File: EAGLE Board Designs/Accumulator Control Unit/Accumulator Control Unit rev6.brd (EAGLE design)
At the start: 255 x 73 mm, 301 parts, among them J1 CONNECTOR-12_MF_T_V_, J2 CONNECTOR-6_μF_T_V_BLACK, J3 CONNECTOR-4_μF_T_V_BLACK, J4 CONNECTOR-2_MF_T_V_, J5 CONNECTOR-8_μF_T_V_BLACK, J6 CONNECTOR-16_MF_T_V_, J9 CONNECTOR-2_MF_T_V_, Q1 TRANSISTOR_N_MOS__PMV15ENEA, Q2 TRANSISTOR_N_MOS__PMV15ENEA, Q3 TRANSISTOR_N_MOS__PMV15ENEA, Q4 TRANSISTOR_N_MOS__PMV15ENEA, T1 TRANSFORMER_HM2112ZNLT_AIRGAP, U1 VOLTAGE_REGULATOR_SOT-223_3.3V, U10 TCAN1051HQV-Q1, U11 OPAMP_1_CHANNEL_OPA991, U12 OPAMP_1_CHANNEL_OPA991, U13 OPAMP_1_CHANNEL_OPA991, U14 RELAY_SOLIDSTATE_NO_DIP-4, U15 LM555, U16 OPAMP_1_CHANNEL_OPA991, U17 OPAMP_2_CHANNEL_OPA_2991, U18 OPAMP_1_CHANNEL_OPA991, U19 OPAMP_2_CHANNEL_OPA_2991, U2 RELAY_SOLIDSTATE_NO_DIP-4, U20 LOGICGATE_BUFFER, U21 ADM8316WBX30, U22 OPAMP_1_CHANNEL_OPA991, U23 LOGICGATE_AND_DCK3, U24 LOGICGATE_AND_DCK3, U25 LOGICGATE_AND_DCK3, U26 OPAMP_1_CHANNEL_OPA991, U27 ADG1423, U28 OPAMP_1_CHANNEL_OPA991, U29 OPAMP_2_CHANNEL_OPA_2991, U3 RELAY_SOLIDSTATE_NO_DIP-4, U30 OPAMP_1_CHANNEL_OPA991, U31 OPAMP_2_CHANNEL_OPA_2991, U32 LTC6820, U33 OPAMP_1_CHANNEL_OPA991, U4 OPAMP_1_CHANNEL_OPA991, U5 OPAMP_1_CHANNEL_OPA991, U6 TCAN1051HQV-Q1, U7 LTC6820, U8 OPAMP_1_CHANNEL_OPA991, U9 OPAMP_1_CHANNEL_OPA991

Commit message: acu_rev6_schematic_update
moved precharge control circuit difference amplifiers' pull down resistors to between the differential inputs
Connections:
- net GND: no longer R55.1, R62.1
- net ISO_PACK+: now also R55.2
- net ISO_PACK-: now also R55.1; no longer R55.2
- net ISO_TS+: now also R62.2
- net ISO_TS-: now also R62.1; no longer R62.2
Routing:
- net ISO_TS+: track 23.7 -> 20.8 mm
- net ISO_PACK+: track 24.8 -> 22.1 mm
- net GND: track 544.1 -> 541.5 mm, vias 132 -> 130
- net ISO_PACK-: track 23.8 -> 22.2 mm
- net ISO_TS-: track 21.0 -> 19.6 mm

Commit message: acu-rev6-schematic-update
some changes to precharge control circuit
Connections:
- net HV+_OUT_OK: now also R87.2, U23.4, U25.2; no longer R88.2, U24.4, U25.1
- net PRECHARGE+_OUT_OK: now also R88.2, U24.4, U25.1; no longer R87.2, U23.4, U25.2
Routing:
- net PRECHARGE+_OUT_OK: track 6.56 -> 21.6 mm
- net HV+_OUT_OK: track 21.6 -> 6.56 mm
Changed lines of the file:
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@@
 <wire x1="18.419" y1="8.3488" x2="19.8224" y2="8.3488" width="0.254" layer="1"/>
 </signal>
-<signal name="HV+_OUT_OK">
+<signal name="PRECHARGE+_OUT_OK">
 <contactref element="U24" pad="4"/>
 <contactref element="U25" pad="1"/>
@@
 <wire x1="16.6624" y1="15.7344" x2="16.6624" y2="16.2188" width="0.254" layer="1"/>
 </signal>
-<signal name="PRECHARGE+_OUT_OK">
+<signal name="HV+_OUT_OK">
 <contactref element="U23" pad="4"/>
 <contactref element="U25" pad="2"/>

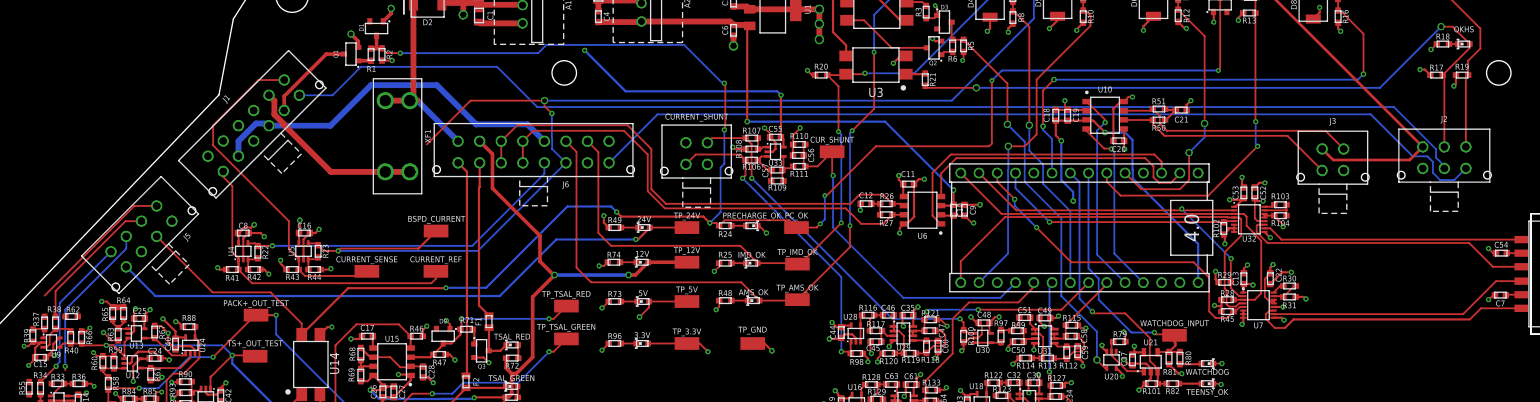
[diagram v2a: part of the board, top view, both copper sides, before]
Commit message: some routing fixed will do the rest once I get back
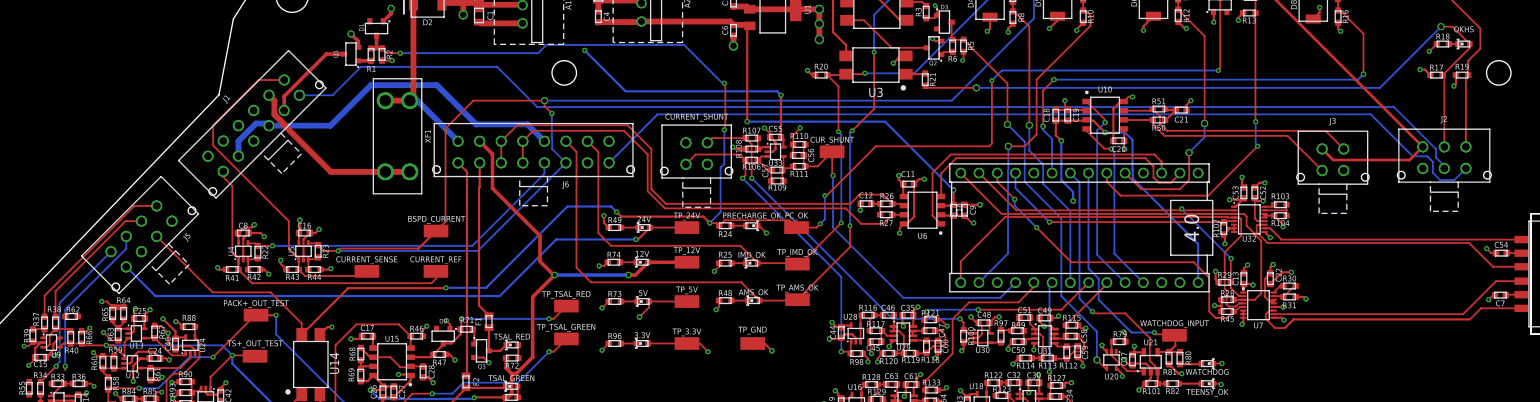
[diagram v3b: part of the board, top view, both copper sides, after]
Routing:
- net BSPD_CURRENT: track 168.9 -> 180.1 mm
- net ISO_TS+: track 20.8 -> 23.7 mm
- net 24VIN: track 27.3 -> 26.3 mm
- net WATCHDOG_INPUT: track 37.3 -> 36.7 mm
- net GND: track 541.5 -> 542.1 mm

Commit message: fixed all drc errrors again
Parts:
- moved R62 3.35 mm to (9.27, 24.8)
- moved R55 1.15 mm to (7.24, 14.3), turned to 0 degrees
- moved R34 1.04 mm to (7.24, 12.8), turned to 0 degrees
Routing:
- net ISO_PACK+: track 22.1 -> 26.3 mm
- net +24V: track 392.5 -> 388.4 mm
- net ISO_PACK-: track 22.2 -> 25.3 mm
- net GND: track 542.1 -> 542.8 mm

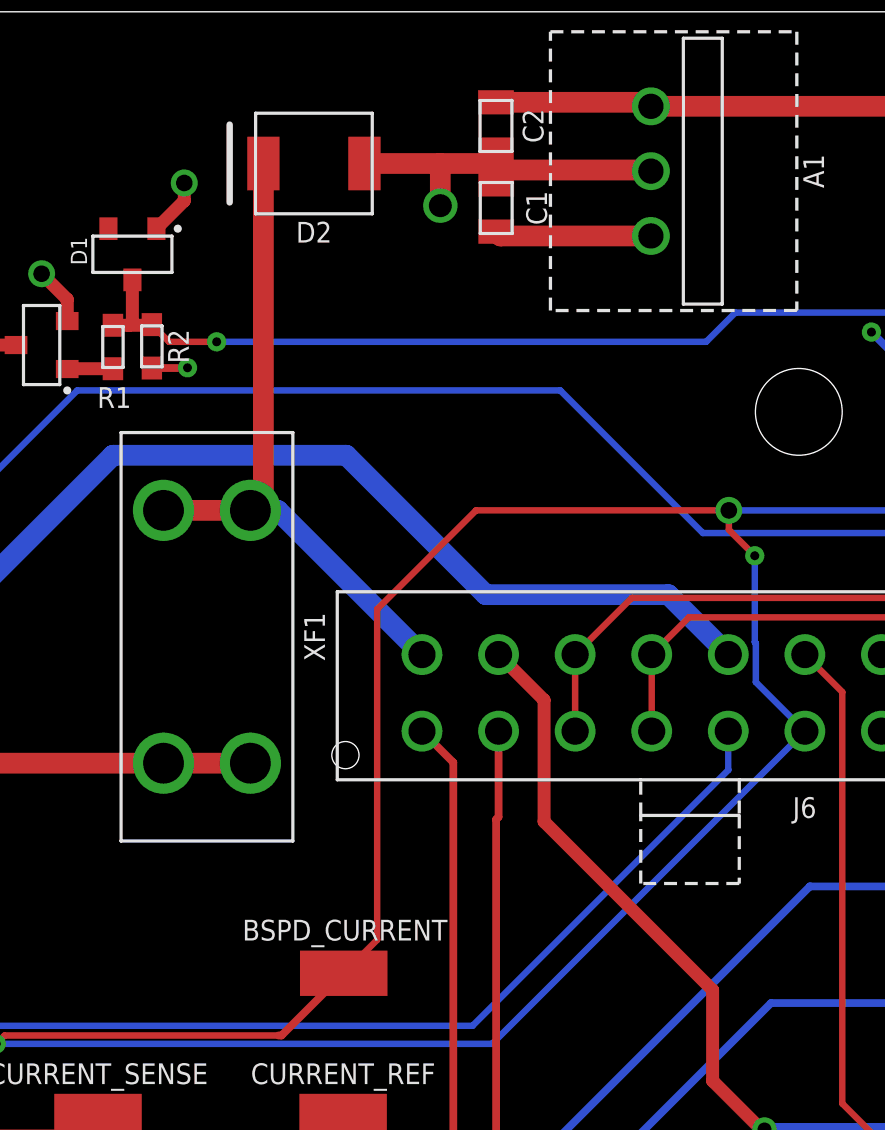
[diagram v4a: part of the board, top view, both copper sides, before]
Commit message: Added RPP with mosfet need to double check
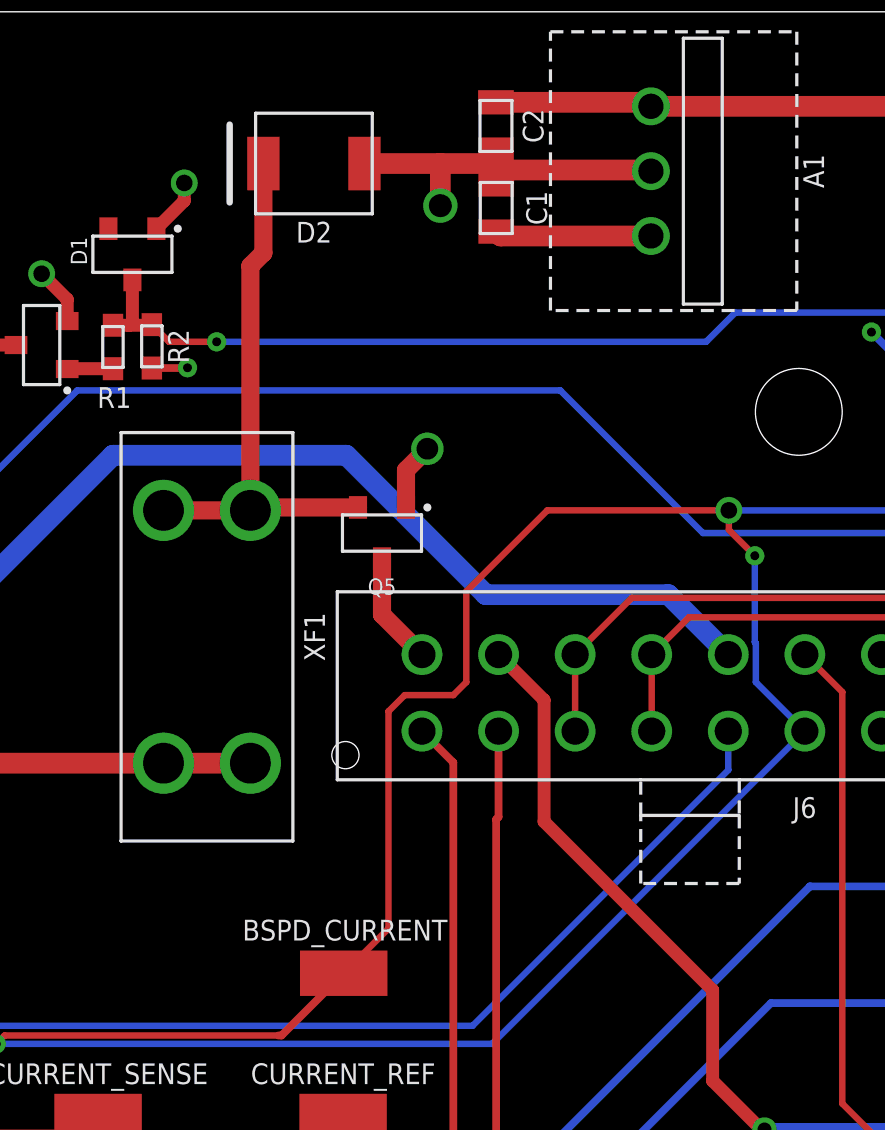
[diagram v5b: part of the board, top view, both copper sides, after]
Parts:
- added Q5: TRANSISTOR_P_MOS_SOT-23_DMP3056L-7, HyTechDevices:SOT-23
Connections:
- new net N$75: D2.2, Q5.2, XF1.1, XF1.2
- net 24VIN: now also Q5.3; no longer D2.2, XF1.1, XF1.2
- net GND: now also Q5.1
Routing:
- net 24VIN: track 26.3 -> 4.41 mm
- net N$75: track 0.00 -> 21.5 mm
- net GND: track 542.8 -> 545.4 mm, vias 130 -> 131
- net BSPD_CURRENT: track 180.1 -> 179.6 mm
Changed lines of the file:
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@@
 <attribute name="VOLTAGE_MAX" value="75V" x="138.1506" y="37.084" size="1.778" layer="27" rot="R180" display="off"/>
 </element>
+<element name="Q5" library="HyTechDevices" package="SOT-23" value="TRANSISTOR_P_MOS_SOT-23_DMP3056L-7" x="64.516" y="52.578" smashed="yes" rot="R180">
+<attribute name="DKPN" value="DMP3056L-7DITR-ND" x="64.516" y="52.578" size="1.778" layer="27" rot="R180" display="off"/>
+<attribute name="MANUFACTURER" value="Diodes Incorporated" x="64.516" y="52.578" size="1.778" layer="27" rot="R180" display="off"/>
+<attribute name="MOPN" value="621-DMP3056L-7" x="64.516" y="52.578" size="1.778" layer="27" rot="R180" display="off"/>
+<attribute name="MPN" value="DMP3056L-7" x="64.516" y="52.578" size="1.778" layer="27" rot="R180" display="off"/>
+<attribute name="NAME" x="64.516" y="50.8" size="0.635" layer="25" font="vector" align="top-center"/>
+</element>
 </elements>
 <signals>
@@
 <wire x1="137.553" y1="36.449" x2="137.795" y2="36.449" width="0.254" layer="1"/>
 <via x="137.795" y="36.449" extent="1-16" drill="0.35"/>
+<contactref element="Q5" pad="1"/>
+<wire x1="65.4558" y1="53.5813" x2="65.4558" y2="55.0418" width="0.7112" layer="1"/>
+<wire x1="65.4558" y1="55.0418" x2="66.294" y2="55.88" width="0.7112" layer="1"/>
+<via x="66.294" y="55.88" extent="1-16" drill="0.85"/>
 </signal>
 <signal name="+12V">
@@
 <wire x1="49.403" y1="32.5656" x2="49.7304" y2="32.893" width="0.254" layer="1"/>
 <wire x1="49.7304" y1="32.893" x2="60.452" y2="32.893" width="0.254" layer="1"/>
-<wire x1="64.3276" y1="49.5956" x2="68.199" y2="53.467" width="0.254" layer="1"/>
-<wire x1="68.199" y1="53.467" x2="78.105" y2="53.467" width="0.254" layer="1"/>
 <via x="78.105" y="53.467" extent="1-16" drill="0.65"/>
+<wire x1="70.993" y1="53.467" x2="78.105" y2="53.467" width="0.254" layer="1"/>
 <wire x1="78.105" y1="53.467" x2="134.747" y2="53.467" width="0.254" layer="16"/>
 <wire x1="134.747" y1="53.467" x2="146.177" y2="64.897" width="0.254" layer="16"/>
@@
 <wire x1="79.121" y1="51.689" x2="78.105" y2="52.705" width="0.254" layer="1"/>
 <wire x1="78.105" y1="52.705" x2="78.105" y2="53.467" width="0.254" layer="1"/>
-<wire x1="64.3276" y1="36.6416" x2="64.3276" y2="49.5956" width="0.254" layer="1"/>
-<wire x1="63.0174" y1="35.3314" x2="64.3276" y2="36.6416" width="0.254" layer="1"/>
+<wire x1="67.818" y1="50.292" x2="70.993" y2="53.467" width="0.254" layer="1"/>
+<wire x1="64.77" y1="37.084" x2="64.77" y2="45.593" width="0.254" layer="1"/>
+<wire x1="64.77" y1="45.593" x2="65.405" y2="46.228" width="0.254" layer="1"/>
+<wire x1="65.405" y1="46.228" x2="67.31" y2="46.228" width="0.254" layer="1"/>
+<wire x1="67.31" y1="46.228" x2="67.818" y2="46.736" width="0.254" layer="1"/>
+<wire x1="63.0174" y1="35.3314" x2="64.77" y2="37.084" width="0.254" layer="1"/>
+<wire x1="67.818" y1="46.736" x2="67.818" y2="50.292" width="0.254" layer="1"/>
 </signal>
 <signal name="IMD_OK">
@@
 </signal>
 <signal name="24VIN">
-<contactref element="XF1" pad="1"/>
-<contactref element="XF1" pad="2"/>
-<contactref element="D2" pad="2"/>
 <contactref element="J6" pad="1"/>
-<wire x1="59.869" y1="67.056" x2="59.869" y2="53.9762" width="0.8128" layer="1"/>
-<wire x1="59.869" y1="53.9762" x2="59.3598" y2="53.467" width="0.8128" layer="1"/>
-<wire x1="66.083" y1="47.817" x2="60.433" y2="53.467" width="0.8128" layer="16"/>
-<wire x1="59.3598" y1="53.467" x2="55.9562" y2="53.467" width="0.8128" layer="1"/>
-<wire x1="60.433" y1="53.467" x2="59.3598" y2="53.467" width="0.8128" layer="16"/>
+<contactref element="Q5" pad="3"/>
+<wire x1="66.083" y1="47.817" x2="64.516" y2="49.384" width="0.7112" layer="1"/>
+<wire x1="64.516" y1="49.384" x2="64.516" y2="51.5747" width="0.7112" layer="1"/>
 </signal>
 <signal name="TIMER_EN">
@@
 <wire x1="126.016" y1="11.105" x2="126.833" y2="11.105" width="0.254" layer="1"/>
 </signal>
+<signal name="N$75">
+<contactref element="Q5" pad="2"/>
+<contactref element="D2" pad="2"/>
+<contactref element="XF1" pad="1"/>
+<contactref element="XF1" pad="2"/>
+<wire x1="63.5762" y1="53.5813" x2="59.4741" y2="53.5813" width="0.7112" layer="1"/>
+<wire x1="55.9562" y1="53.467" x2="59.3598" y2="53.467" width="0.7112" layer="1"/>
+<wire x1="59.3598" y1="53.467" x2="59.4741" y2="53.5813" width="0.7112" layer="1"/>
+<wire x1="59.3598" y1="53.467" x2="59.3598" y2="63.0428" width="0.7112" layer="1"/>
+<wire x1="59.869" y1="63.552" x2="59.869" y2="67.056" width="0.7112" layer="1"/>
+<wire x1="59.3598" y1="63.0428" x2="59.869" y2="63.552" width="0.7112" layer="1"/>
+</signal>
 </signals>

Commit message: some more changes
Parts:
- moved R18 10.5 mm to (198.1, 52.1)
- moved OKHS 10.5 mm to (201.2, 52.1)
- moved J2 0.26 mm to (203.2, 43.8)
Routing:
- net OKHS: track 96.4 -> 84.6 mm
- net +12V: track 205.4 -> 200.8 mm
- net MHS: track 43.2 -> 38.8 mm
- net PRECHARGE_OK: track 267.5 -> 263.4 mm
- net GND: track 545.4 -> 544.5 mm, vias 131 -> 130
- net +5V: track 319.1 -> 318.5 mm
- net ACCUMULATOR_GND: track 168.4 -> 167.9 mm
